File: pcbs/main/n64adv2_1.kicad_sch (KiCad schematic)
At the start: 74 parts, among them Q1 2N2222, Q2 2N2222, Q3 2N2222, U1 10M16SAE144/10M25SAE144, U2 ADV7513, U3 AS4C8M16SA-xTCN, U4 SI5356A-B-GMR, U5 ASE-50.000MHZ-LC-T, U6 ASE-24.576MHZ-LC-T, U7 74LVC2G17DBV, X1 3-1734592-0, X2 3020-10-0300-00, X3 2000-1-2-41-00-BK, X4 TEI0005, X5 USB3140-30-0170-0-C, Y41 7A-27.000MAAJ-T

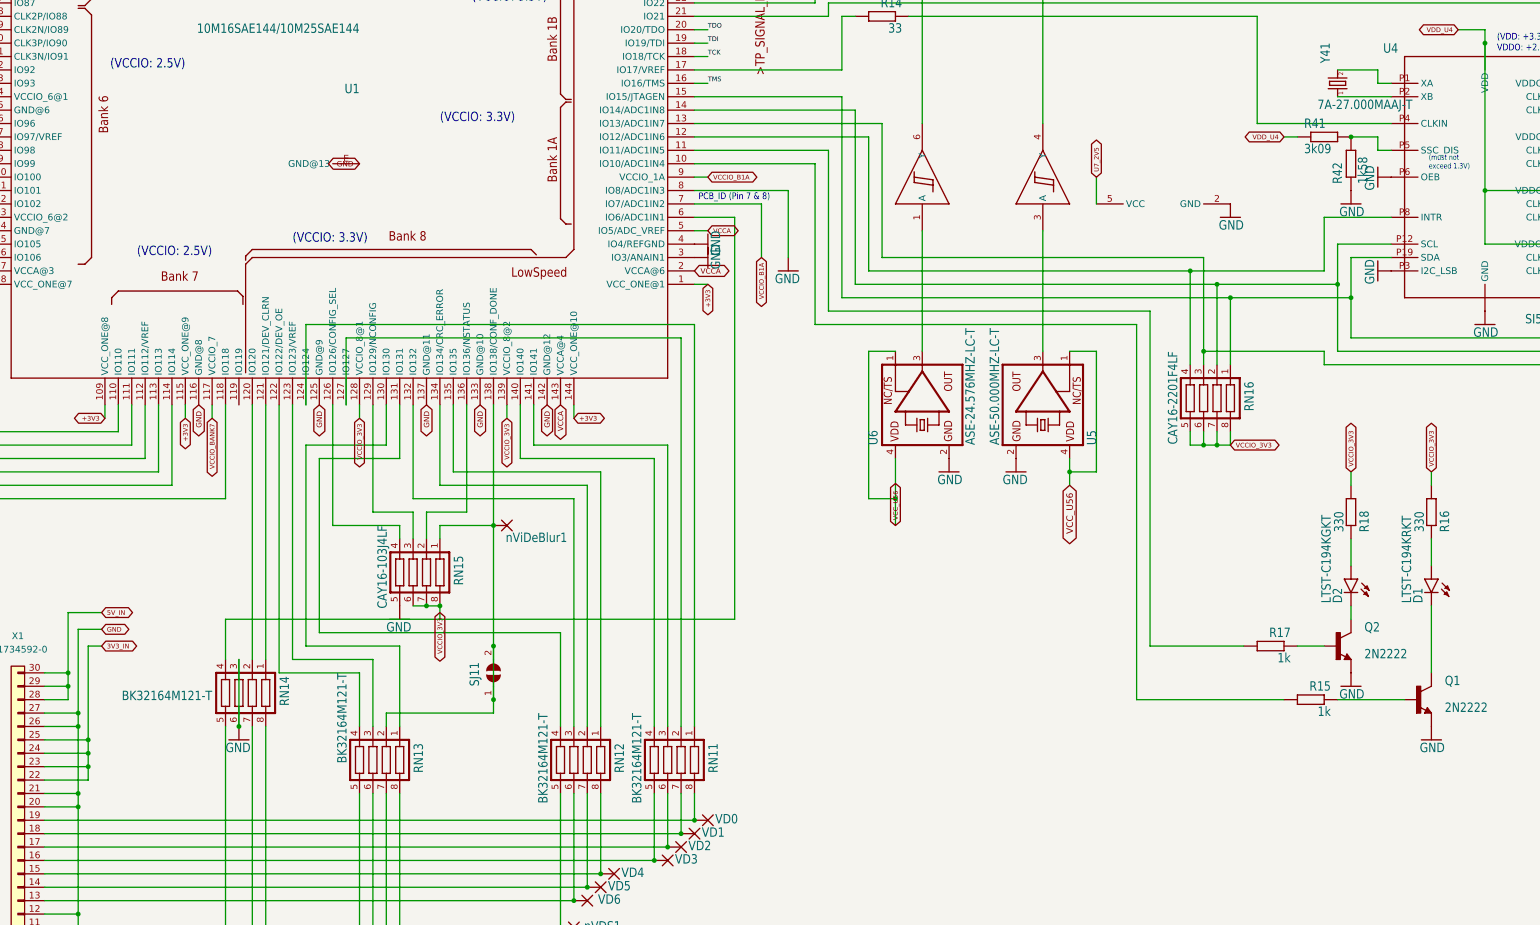
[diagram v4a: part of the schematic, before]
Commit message: update part numbers for Y41,, RN11-14
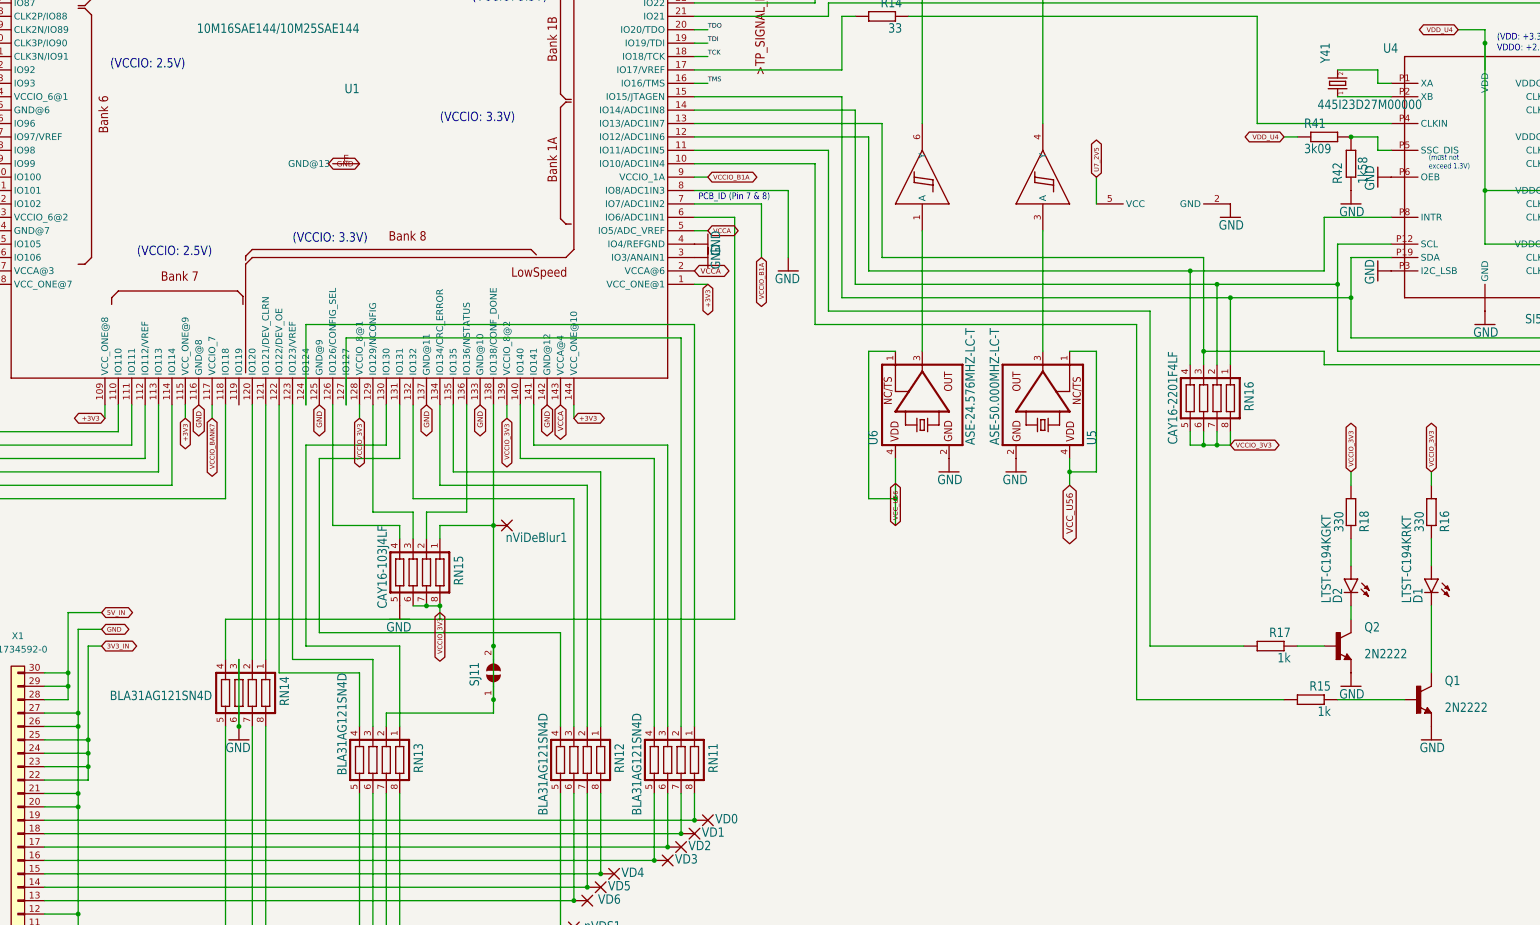
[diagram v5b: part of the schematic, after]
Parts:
- RN11, RN12, RN13, RN14: value BK32164M121-T -> BLA31AG121SN4D
- Y41: value 7A-27.000MAAJ-T -> 445I23D27M00000
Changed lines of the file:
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@@
       (effects (font (size 1.778 1.5113)) (justify left bottom))
     )
-    (property "Value" "BK32164M121-T" (id 1) (at 248.92 270.002 90)
+    (property "Value" "BLA31AG121SN4D" (id 1) (at 248.92 270.002 90)
       (effects (font (size 1.778 1.5113)) (justify right top))
     )
@@
       (effects (font (size 1.778 1.5113)) (justify left bottom))
     )
-    (property "Value" "BK32164M121-T" (id 1) (at 328.422 274.32 0)
+    (property "Value" "BLA31AG121SN4D" (id 1) (at 328.422 274.32 0)
       (effects (font (size 1.778 1.5113)) (justify left bottom))
     )
@@
       (effects (font (size 1.778 1.5113)) (justify left bottom))
     )
-    (property "Value" "BK32164M121-T" (id 1) (at 310.642 274.32 0)
+    (property "Value" "BLA31AG121SN4D" (id 1) (at 310.642 274.32 0)
       (effects (font (size 1.778 1.5113)) (justify left bottom))
     )
@@
       (effects (font (size 1.778 1.5113)) (justify left bottom))
     )
-    (property "Value" "7A-27.000MAAJ-T" (id 1) (at 458.47 160.02 90)
+    (property "Value" "445I23D27M00000" (id 1) (at 458.47 160.02 90)
       (effects (font (size 1.778 1.5113)) (justify right top))
     )
@@
       (effects (font (size 1.778 1.5113)) (justify left bottom))
     )
-    (property "Value" "BK32164M121-T" (id 1) (at 272.542 266.7 0)
-      (effects (font (size 1.778 1.5113)) (justify left bottom))
-    )
+    (property "Value" "BLA31AG121SN4D" (id 1) (at 272.542 266.7 0)
+      (effects (font (size 1.778 1.5113)) (justify left bottom))
+    )

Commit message: update main-pcb: - remove jumper which were left overs from prototype stages - remove some test points - add pads for SPDIF near DIY-IO-Pad area
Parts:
- removed R41: 3k09, n64adv2:R0603, symbol n64adv2-eagle-import:R-EU_R0603
- removed SJ11, SJ31, SJ5, SJ6: SJSMALL, n64adv2:SJ_SMALL, symbol n64adv2-eagle-import:SJSMALL
- removed TP_SCL0, TP_SDA0, TP_SPDIF0: TPB1,27, n64adv2:B1,27, symbol n64adv2-eagle-import:TPB1,27
- removed U7: 74LVC2G17DBV, n64adv2:SOT-23-6, symbol n64adv2-eagle-import:2G17TI_DBV
- added SPDIF1, SPDIF_GND1, SPDIF_VCCIO1: SMD1, n64adv2:SMD0,8-1,6, symbol n64adv2-eagle-import:SMD1
- R41: renamed from R42; value 1k58 -> 1k
- U5: value ASE-50.000MHZ-LC-T -> ECS-3225MV-500-CN-TR
- U6: value ASE-24.576MHZ-LC-T -> ECS-3225MVLC-245.7-CN-TR
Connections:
- net VCCIO_BANK7 is gone; now on net VCCIO_BANK67: U1.117 (VCCIO_7)
- net GND: now also R41.2, U1.7 (IO7/ADC1IN2), SPDIF_GND1.P$1 (P); no longer R41.1, U1.8 (IO8/ADC1IN3)
- net VCCIO_3V3: now also SPDIF_VCCIO1.P$1 (P)
- net VCCIO_B1A: now also U1.8 (IO8/ADC1IN3); no longer U1.7 (IO7/ADC1IN2)
- net at U4.P5 (SSC_DIS): now also R41.1; no longer R41.2
- net at U5.3 (OUT): now also U1.27 (CLK0P/I27)
- net at U1.25 (IO25): now also SPDIF1.P$1 (P)
- net at U1.26 (CLK0N/I26): now also U6.3 (OUT)
- net CLK_CIRCUIT_2V5 renamed VCCIO_U4
- net VCCIO_2V5 renamed VCCIO_BANK234
- net VCCIO_BANK6 renamed VCCIO_BANK67
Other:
- note added: "Pin40: n.c."
- title: N64Adv2 (ADV7513) -> N64Adv2
- moved on the sheet: C4, D1, D2, Q1, Q2, Q3, R11, R12, R13, R15, R16, R17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
